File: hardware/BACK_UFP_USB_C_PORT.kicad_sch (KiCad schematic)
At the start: 26 parts, among them J5 USB4200-03-A (VIRT FLAG MOUNT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, Q18 PMOS, Q19 PMOS, Q20 PMOS, Q21 PMOS

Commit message: working on hardware
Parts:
- added C91, C92, C93, C94: 0.1uF, Capacitor_SMD:C_0603_1608Metric, symbol Device:C
- C90: renamed from C83; footprint (none) -> Capacitor_SMD:C_0603_1608Metric
- C95: renamed from C85; footprint (none) -> Capacitor_SMD:C_0603_1608Metric
- C96: renamed from C82; footprint (none) -> Capacitor_SMD:C_0603_1608Metric
- C97: renamed from C80; footprint (none) -> Capacitor_SMD:C_0603_1608Metric
- C98: renamed from C81; footprint (none) -> Capacitor_SMD:C_0603_1608Metric
- C99: renamed from C84; footprint (none) -> Capacitor_SMD:C_0603_1608Metric
- JP10: renamed from JP6; footprint (none) -> Jumper:SolderJumper-3_P1.3mm_Open_RoundedPad1.0x1.5mm_NumberLabels
- JP11: renamed from JP5; footprint (none) -> Jumper:SolderJumper-3_P1.3mm_Open_RoundedPad1.0x1.5mm_NumberLabels
- JP12: renamed from JP2; footprint (none) -> Jumper:SolderJumper-3_P1.3mm_Open_RoundedPad1.0x1.5mm_NumberLabels
- JP13: renamed from JP1; footprint (none) -> Jumper:SolderJumper-3_P1.3mm_Open_RoundedPad1.0x1.5mm_NumberLabels
- JP9: renamed from JP7; footprint (none) -> Jumper:SolderJumper-3_P1.3mm_Open_RoundedPad1.0x1.5mm_NumberLabels
- Q18: footprint (none) -> CARTHING:TRANS_PMPB11EN_115
- Q19: renamed from Q21; footprint (none) -> CARTHING:TRANS_PMPB11EN_115
- Q20: renamed from Q19; footprint (none) -> CARTHING:TRANS_PMPB11EN_115
- Q21: renamed from Q20; footprint (none) -> CARTHING:TRANS_PMPB11EN_115
- TP4: renamed from TP1; footprint (none) -> TestPoint:TestPoint_Pad_D1.5mm
- renumbered J5 to J7, R91 to R90, R92 to R91, R90 to R92, U12 to U13, U14 to U15
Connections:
- net UFP_3_TXA_N: now also C91.2; no longer J7.A3 (TX1-)
- net UFP_3_TXA_P: now also C92.1; no longer J7.A2 (TX1+)
- net UFP_3_TXB_N: now also C93.2; no longer J7.B3 (TX2-)
- net UFP_3_TXB_P: now also C94.1; no longer J7.B2 (TX2+)
- net at U15.8 (VCONN_IN): now also C99.1, JP11.2 (C)
- new net: C92.2, J7.A2 (TX1+)
- new net: C91.1, J7.A3 (TX1-)
- new net: C94.2, J7.B2 (TX2+)
- new net: C93.1, J7.B3 (TX2-)
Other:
- note added: "BACK USB-C PORT CONTROLER"
- note added: "ESD PROTECTION"
- note added: "HUB CHIP UFP BLOCK"
- note added: "PHISICAL USB-C UPSTEAM PORT"
- moved on the sheet: C90, C95, C96, C97, C98, C99, D11, J7, JP10, JP11, JP12, JP13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

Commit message: working assighning footprints still
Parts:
- R89, R90, R91, R92, R93: footprint (none) -> Resistor_SMD:R_0603_1608Metric
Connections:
- net at U15.8 (VCONN_IN): now also C99.1, JP11.2 (C)
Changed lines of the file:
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@@
       (effects (font (size 1.27 1.27)))
     )
-    (property "Footprint" "" (at 171.45 154.178 90)
+    (property "Footprint" "Resistor_SMD:R_0603_1608Metric" (at 171.45 154.178 90)
       (effects (font (size 1.27 1.27)) hide)
     )
@@
       (effects (font (size 1.27 1.27)) (justify left))
     )
-    (property "Footprint" "" (at 66.802 170.18 90)
+    (property "Footprint" "Resistor_SMD:R_0603_1608Metric" (at 66.802 170.18 90)
       (effects (font (size 1.27 1.27)) hide)
     )
@@
       (effects (font (size 1.27 1.27)) (justify left))
     )
-    (property "Footprint" "" (at 187.452 119.38 90)
+    (property "Footprint" "Resistor_SMD:R_0603_1608Metric" (at 187.452 119.38 90)
       (effects (font (size 1.27 1.27)) hide)
     )
@@
       (effects (font (size 1.27 1.27)))
     )
-    (property "Footprint" "" (at 171.45 128.778 90)
+    (property "Footprint" "Resistor_SMD:R_0603_1608Metric" (at 171.45 128.778 90)
       (effects (font (size 1.27 1.27)) hide)
     )
@@
       (effects (font (size 1.27 1.27)) (justify left))
     )
-    (property "Footprint" "" (at 187.452 144.78 90)
-      (effects (font (size 1.27 1.27)) hide)
-    )
+    (property "Footprint" "Resistor_SMD:R_0603_1608Metric" (at 187.452 144.78 90)
+      (effects (font (size 1.27 1.27)) hide)
+    )

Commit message: FINALY starting the pcb
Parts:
- D11: footprint (none) -> CARTHING:PUSB3AB6Z_NEX
- J7: footprint (none) -> CARTHING:USB4200-03-A_REVA
- U13: footprint (none) -> CARTHING:VQFN100_KD_MCH
- U15: footprint (none) -> CARTHING:PTN5100BSMP
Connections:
- net at U15.8 (VCONN_IN): now also C99.1, JP11.2 (C)
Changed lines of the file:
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@@
       (effects (font (size 1.27 1.27)))
     )
-    (property "Footprint" "" (at 231.14 85.09 0)
+    (property "Footprint" "CARTHING:VQFN100_KD_MCH" (at 231.14 85.09 0)
       (effects (font (size 1.27 1.27)) hide)
     )
@@
       (effects (font (size 1.27 1.27)))
     )
-    (property "Footprint" "" (at 36.83 53.34 0)
+    (property "Footprint" "CARTHING:USB4200-03-A_REVA" (at 36.83 53.34 0)
       (effects (font (size 1.27 1.27)) hide)
     )
@@
       (effects (font (size 1.27 1.27)))
     )
-    (property "Footprint" "" (at 134.62 43.18 0)
+    (property "Footprint" "CARTHING:PUSB3AB6Z_NEX" (at 134.62 43.18 0)
       (effects (font (size 1.27 1.27)) hide)
     )
@@
       (effects (font (size 1.27 1.27)))
     )
-    (property "Footprint" "" (at 96.52 127 0)
+    (property "Footprint" "CARTHING:PTN5100BSMP" (at 96.52 127 0)
       (effects (font (size 1.27 1.27)) hide)
     )
@@
       (effects (font (size 1.27 1.27)))
     )
-    (property "Footprint" "" (at 134.62 15.24 0)
-      (effects (font (size 1.27 1.27)) hide)
-    )
+    (property "Footprint" "CARTHING:PUSB3AB6Z_NEX" (at 134.62 15.24 0)
+      (effects (font (size 1.27 1.27)) hide)
+    )

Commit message: coldent sleep so came back and did somre routing
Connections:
- net at U15.8 (VCONN_IN): now also C99.1, JP11.2 (C)

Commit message: working on routing still  finnished psu section
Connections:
- net at U15.8 (VCONN_IN): now also C99.1, JP11.2 (C)

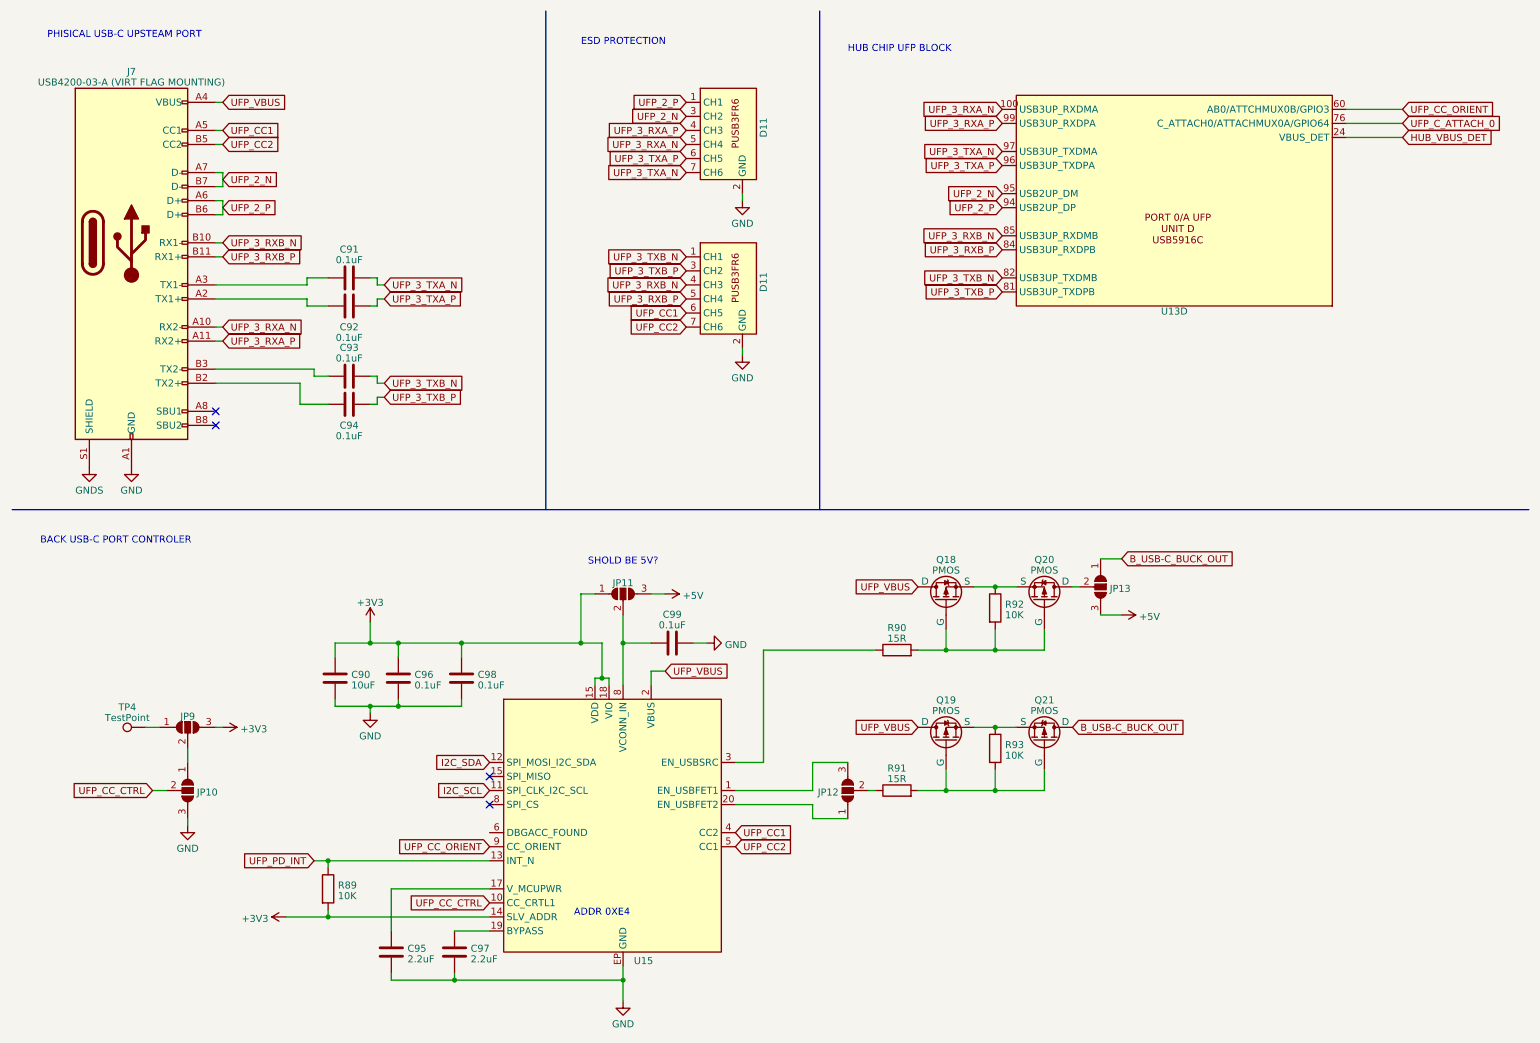
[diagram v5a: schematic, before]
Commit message: worked on usb port and display routing
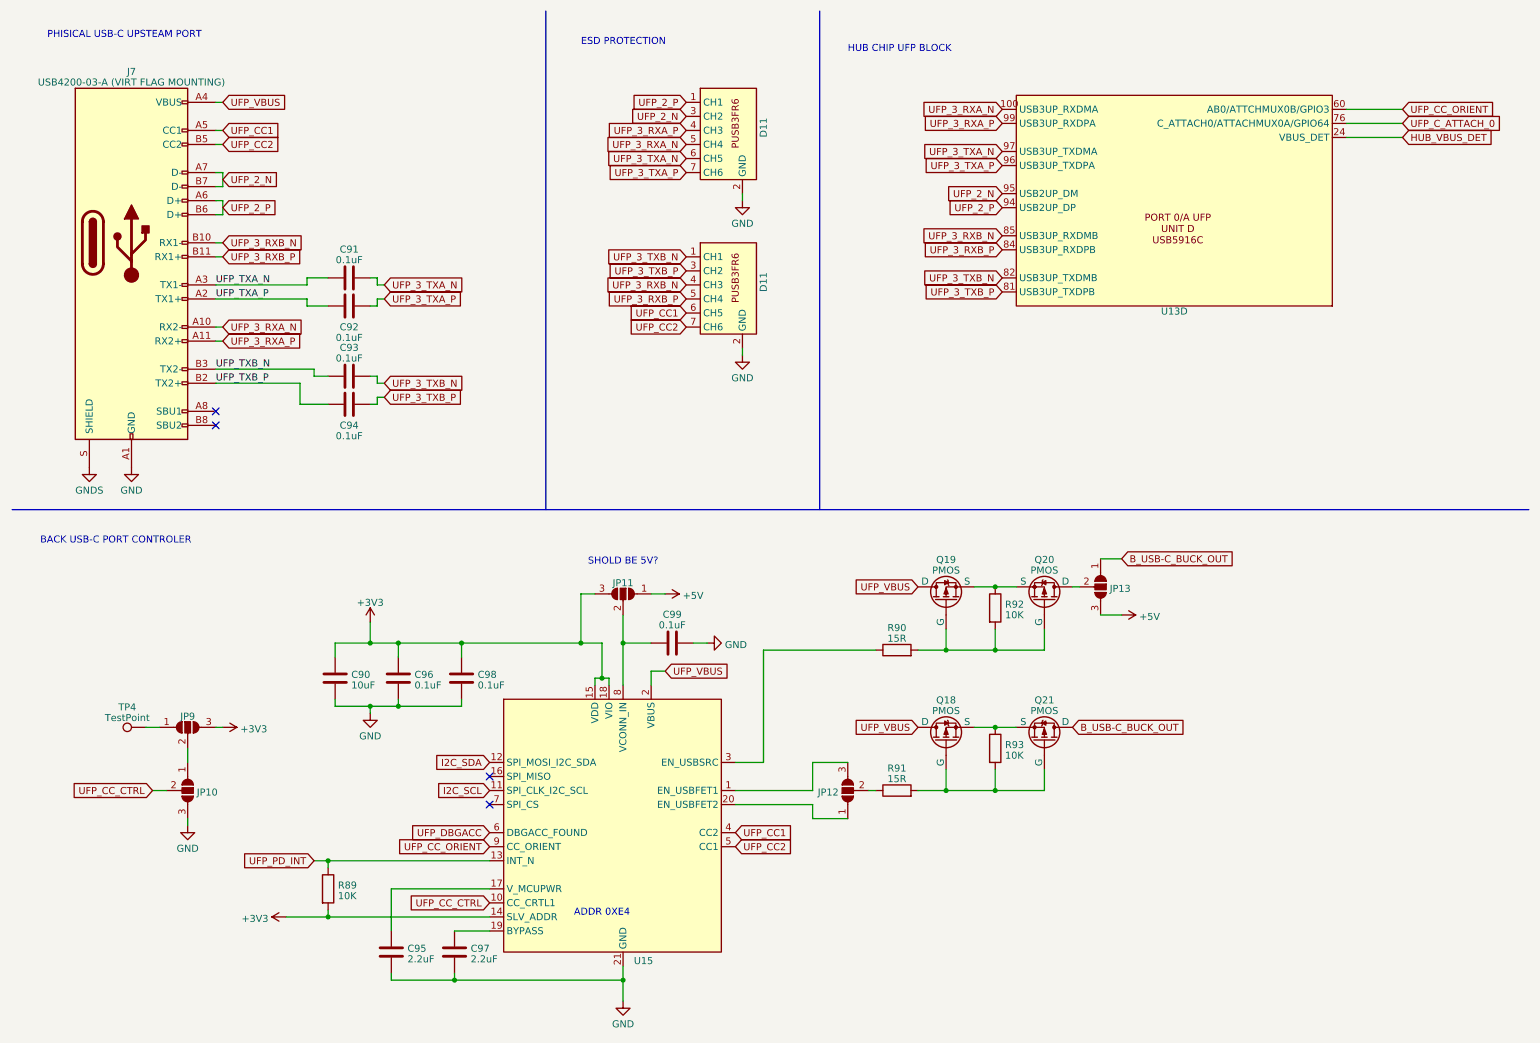
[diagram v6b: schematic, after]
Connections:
- net +3V3: now also JP11.3 (B); no longer JP11.1 (A)
- net +5V: now also JP11.1 (A); no longer JP11.3 (B)
- net B_USB-C_BUCK_OUT: now also Q21.2 (D), Q21.5 (D), Q21.6 (D), Q21.7 (D)
- net GND: now also U15.21 (GND); no longer U15.EP (GND)
- net GNDS: now also J7.S (SHIELD); no longer J7.S1 (SHIELD)
- net UFP_3_TXA_N: now also D11.6 (CH5); no longer D11.7 (CH6)
- net UFP_3_TXA_P: now also D11.7 (CH6); no longer D11.6 (CH5)
- net UFP_VBUS: now also Q18.2 (D), Q18.5 (D), Q18.6 (D), Q18.7 (D), Q19.2 (D), Q19.5 (D), Q19.6 (D), Q19.7 (D)
- net UFP_TXA_P: now reaches C92.2, J7.A2 (TX1+)
- net UFP_TXA_N: now reaches C91.1, J7.A3 (TX1-)
- net UFP_TXB_P: now reaches C94.2, J7.B2 (TX2+)
- net UFP_TXB_N: now reaches C93.1, J7.B3 (TX2-)
- net at R91.2, R93.2: now also Q18.3 (G), Q21.3 (G); no longer Q19.2 (G), Q21.2 (G)
- net UFP_DBGACC: now reaches U15.6 (DBGACC_FOUND)
- net at U15.8 (VCONN_IN): now also C99.1, JP11.2 (C)
- net at JP13.2 (C), Q20.1 (D): now also Q20.2 (D), Q20.5 (D), Q20.6 (D), Q20.7 (D)
- net at R90.2, R92.2: now also Q19.3 (G), Q20.3 (G); no longer Q18.2 (G), Q20.2 (G)
- new net: Q18.4 (S), Q18.8 (S), Q21.4 (S), Q21.8 (S), R93.1
- new net: Q19.4 (S), Q19.8 (S), Q20.4 (S), Q20.8 (S), R92.1

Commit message: working in final routing
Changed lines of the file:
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@@
   (symbol (lib_id "CARTHING:USB5916C") (at 223.52 53.34 180) (unit 4)
     (in_bom yes) (on_board yes) (dnp no)
-    (property "Reference" "U13" (at 221.615 65.7319 0)
+    (property "Reference" "U13" (at 224.79 65.7319 0)
       (effects (font (size 1.27 1.27)))
     )
@@
     )
     (pin "10")
+    (pin "101")
     (pin "17")
     (pin "2")
@@
     (pin "93")
     (pin "98")
-    (pin "EP")
     (pin "1")
     (pin "20")
@@
     (pin "7")
     (pin "70")
-    (pin "76")
+    (pin "73")
     (pin "8")
     (pin "9")
@@
           (reference "U13") (unit 4)
         )
+        (path "/fae025e9-99c5-40c1-af6f-99dc1edbfa43/7a7a6512-c96f-448a-bb8d-4d6e185adf7f"
+          (reference "U13") (unit 4)
+        )

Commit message: finaliseing pcb layout will come back later for a fresh look
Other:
- company: (none) -> MICK MAKE
- title: (none) -> 200W USB PD 3.1 HUB
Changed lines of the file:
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@@
 (kicad_sch (version 20230121) (generator eeschema)
   (paper "A4")
+  (title_block
+    (title "200W USB PD 3.1 HUB")
+    (date "2023-10-03")
+    (rev "A")
+    (company "MICK MAKE")
+    (comment 1 "THIS IS A 2X 100W USB PD SOURCE ")
+    (comment 2 "HUB USB SPEC 3.1")
+    (comment 3 "TOTAL SYSTEM POWER IS ~275w")
+  )
   (junction (at 180.34 152.4) (diameter 0) (color 0 0 0 0)
   )
